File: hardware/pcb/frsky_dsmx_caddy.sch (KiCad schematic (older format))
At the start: 26 parts, among them P1 G9X, P2 Fr-Sky, P3 DSMX, Q1 BC847C, Q2 Si2319DS, Q3 Si2319DS, Q4 BC847C, U1 78L05, U2 LN-6206-30

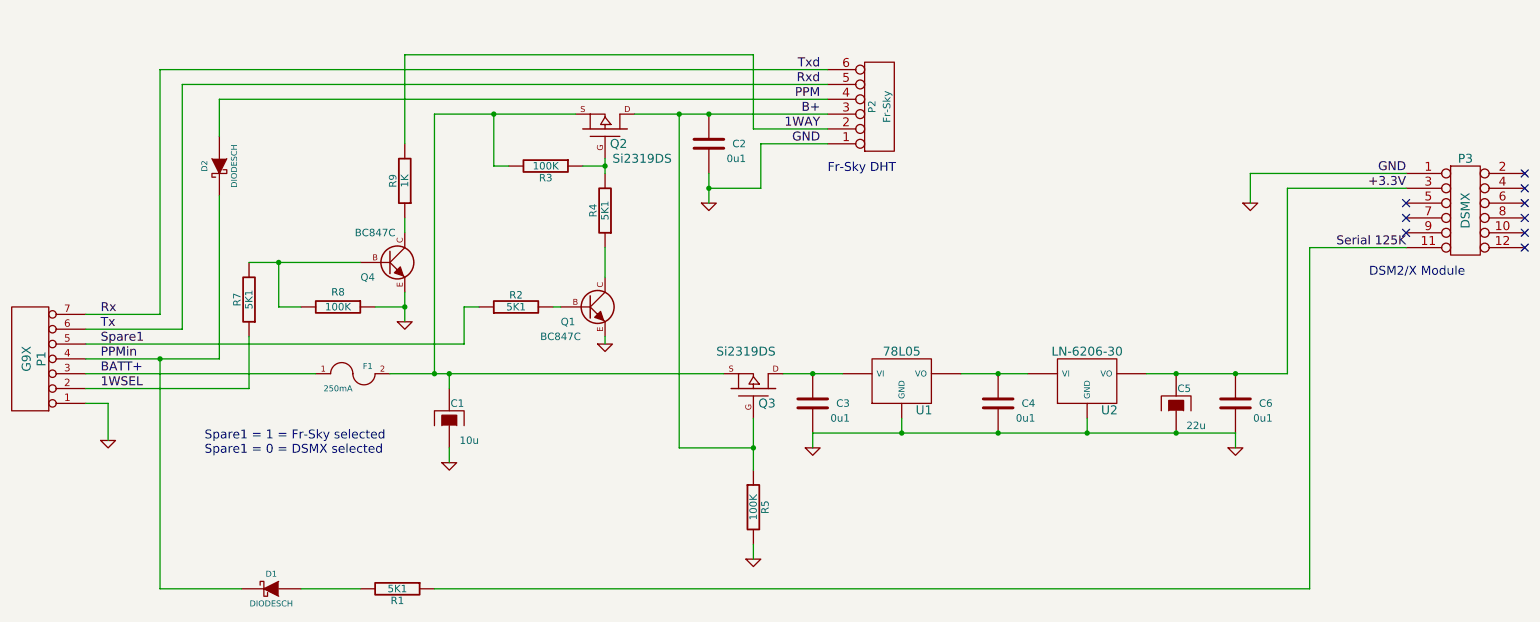
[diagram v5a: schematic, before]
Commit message: TX_CADDY changes to v1.4.
Essentially, this project is a right, royal FAILURE at this time. However,
the circuitry as presented in this commit _appears_ to function correctly
electrically, I have been unable to get the only available DSMX module
to operate. I am unwillingly to break my working DSM2 module in order
to test that it works -- though I presume it would, if the CRO readings
are to be believed.
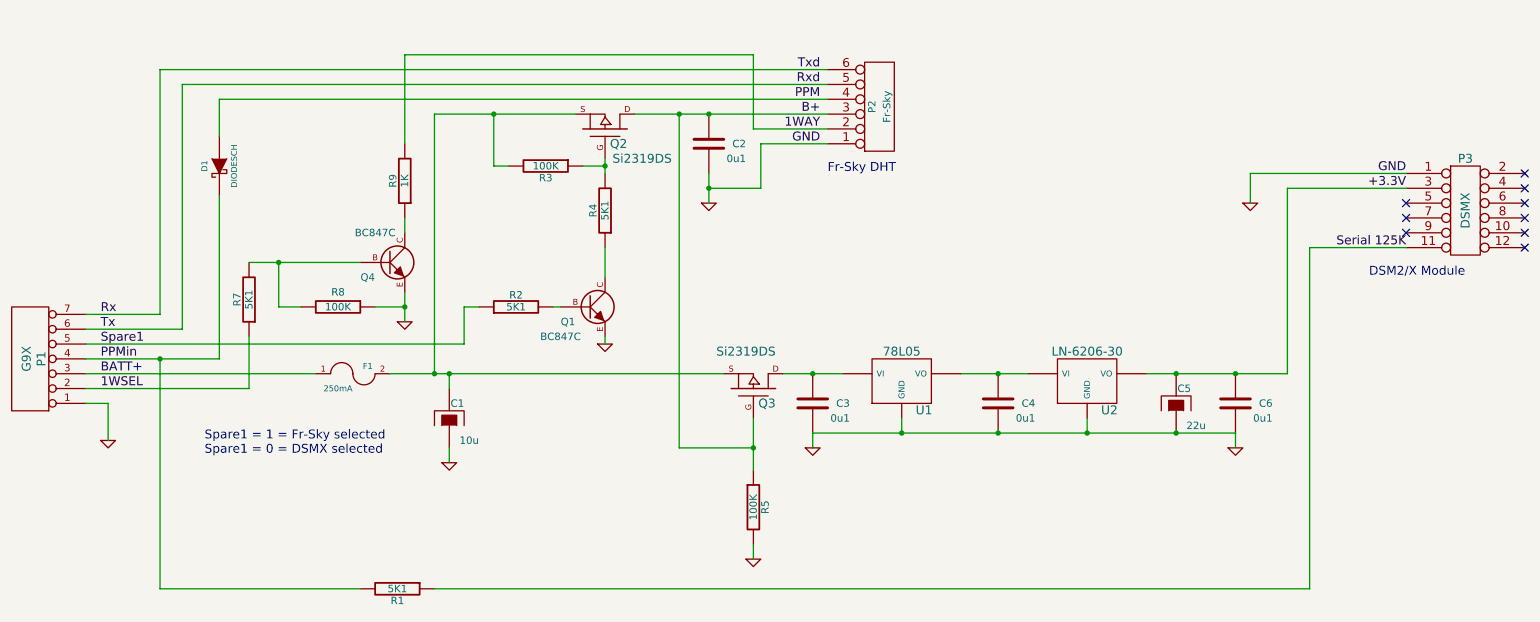
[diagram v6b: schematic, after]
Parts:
- removed D1: DIODESCH, symbol DIODESCH
- renumbered D2 to D1
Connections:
- net PPMin: now also R1.2
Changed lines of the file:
@@
-EESchema Schematic File Version 2  date Wed 24 Oct 2012 07:34:05 PM NZDT
+EESchema Schematic File Version 2  date Wed 24 Oct 2012 09:41:36 PM NZDT
 LIBS:gruvin
 LIBS:power
@@
 Title "Fr-Sky / DSMX TX Moudle Caddy"
 Date "24 oct 2012"
-Rev "1.3"
+Rev "1.4"
 Comp ""
 Comment1 ""
@@
 $EndDescr
 Wire Wire Line
+	1750 3400 1750 4950
+Wire Wire Line
+	1750 4950 3100 4950
+Connection ~ 5750 4000
+Wire Wire Line
+	5750 4000 5250 4000
+Wire Wire Line
+	5750 4150 5750 3800
+Wire Wire Line
+	4450 3050 4400 3050
+Wire Wire Line
+	5550 3500 3300 3500
+Connection ~ 3400 3050
+Wire Wire Line
+	3200 3050 3400 3050
+Wire Wire Line
+	6250 1850 5750 1850
+Wire Wire Line
+	5750 1850 5750 1350
+Wire Wire Line
+	5750 1350 3400 1350
+Wire Wire Line
+	3400 1350 3400 1950
+Wire Wire Line
+	3400 2550 3400 2450
+Wire Wire Line
+	3400 3150 3400 2950
+Wire Wire Line
+	6250 1950 5800 1950
+Connection ~ 4000 1750
+Wire Wire Line
+	4000 1750 4000 2100
+Wire Wire Line
+	4000 2100 4100 2100
+Wire Wire Line
+	5800 1950 5800 2250
+Wire Wire Line
+	6750 3800 6750 3900
+Connection ~ 5450 1750
+Wire Wire Line
+	5800 2250 5450 2250
+Wire Wire Line
+	1400 3950 1400 3700
+Wire Wire Line
+	1400 3700 1250 3700
+Wire Wire Line
+	5950 3500 6350 3500
+Wire Wire Line
+	2150 1900 2150 1650
+Connection ~ 8000 3900
+Wire Wire Line
+	10150 2250 9350 2250
+Wire Wire Line
+	9350 2250 9350 3500
+Wire Wire Line
+	1250 3200 1900 3200
+Wire Wire Line
+	1900 3200 1900 1550
+Wire Wire Line
+	1900 1550 6250 1550
+Wire Wire Line
+	1250 3400 2150 3400
+Wire Wire Line
+	2150 1650 6250 1650
+Connection ~ 4750 2100
+Wire Wire Line
+	4600 2100 4750 2100
+Connection ~ 3600 3500
+Wire Wire Line
+	3600 3500 3600 1750
+Connection ~ 7400 3500
+Wire Wire Line
+	8000 3900 8000 3800
+Wire Wire Line
+	4950 1750 6250 1750
+Connection ~ 7400 3900
+Connection ~ 6150 3500
+Connection ~ 6750 3900
+Wire Wire Line
+	4750 2150 4750 2050
+Wire Wire Line
+	3600 1750 4550 1750
+Wire Wire Line
+	9350 3500 8400 3500
+Wire Wire Line
+	3700 3600 3700 3500
+Wire Wire Line
+	7150 3500 7600 3500
+Connection ~ 3700 3500
+Wire Wire Line
+	1250 3500 2800 3500
+Wire Wire Line
+	1250 3100 1750 3100
+Wire Wire Line
+	1750 3100 1750 1450
+Wire Wire Line
+	1750 1450 6250 1450
+Wire Wire Line
+	9100 2350 9100 2150
+Wire Wire Line
+	9100 2150 10150 2150
+Wire Wire Line
+	2150 3400 2150 2300
+Connection ~ 1750 3400
+Wire Wire Line
+	9000 3900 6150 3900
+Connection ~ 9000 3500
+Connection ~ 8600 3500
+Connection ~ 8600 3900
+Wire Wire Line
+	3700 4000 3700 4100
+Wire Wire Line
+	9000 3900 9000 4000
+Wire Wire Line
+	6150 3900 6150 4000
+Connection ~ 5450 2250
+Wire Wire Line
+	5450 2350 5450 2150
+Wire Wire Line
+	1250 3300 3800 3300
+Wire Wire Line
+	3900 3050 3800 3050
+Wire Wire Line
+	10150 2650 9500 2650
+Wire Wire Line
+	9500 2650 9500 4950
+Wire Wire Line
+	9500 4950 3600 4950
+Wire Wire Line
+	1250 3600 2350 3600
+Wire Wire Line
+	2350 3600 2350 3250
+Wire Wire Line
+	2350 2750 3100 2750
+Wire Wire Line
+	2700 3050 2550 3050
+Wire Wire Line
+	2550 3050 2550 2750
+Connection ~ 2550 2750
+Wire Wire Line
+	3800 3050 3800 3300
+Wire Wire Line
+	4750 3250 4750 3300
+Wire Wire Line
+	4750 2650 4750 2850
+Wire Wire Line
+	5250 4000 5250 1750
+Connection ~ 5250 1750
+Wire Wire Line
 	5750 4750 5750 4650
-Connection ~ 5250 1750
-Wire Wire Line
-	5250 1750 5250 4000
-Wire Wire Line
-	4750 2650 4750 2850
-Wire Wire Line
-	4750 3250 4750 3300
-Wire Wire Line
-	3800 3050 3800 3300
-Connection ~ 2550 2750
-Wire Wire Line
-	2550 2750 2550 3050
-Wire Wire Line
-	2550 3050 2700 3050
-Wire Wire Line
-	2350 2750 2550 2750
-Wire Wire Line
-	2550 2750 3100 2750
-Wire Wire Line
-	2350 3250 2350 3600
-Wire Wire Line
-	2350 3600 1250 3600
-Wire Wire Line
-	3600 4950 9500 4950
-Wire Wire Line
-	9500 4950 9500 2650
-Wire Wire Line
-	9500 2650 10150 2650
-Wire Wire Line
-	3800 3050 3900 3050
-Wire Wire Line
-	3800 3300 1250 3300
-Wire Wire Line
-	5450 2350 5450 2250
-Wire Wire Line
-	5450 2250 5450 2150
-Connection ~ 5450 2250
-Wire Wire Line
-	6150 4000 6150 3900
-Wire Wire Line
-	9000 4000 9000 3900
-Wire Wire Line
-	3700 4000 3700 4100
-Wire Wire Line
-	1750 3400 1750 4950
-Wire Wire Line
-	1750 4950 2300 4950
-Connection ~ 8600 3900
-Connection ~ 8600 3500
-Connection ~ 9000 3500
-Wire Wire Line
-	9000 3900 8600 3900
-Wire Wire Line
-	8600 3900 8000 3900
-Wire Wire Line
-	8000 3900 7400 3900
-Wire Wire Line
-	7400 3900 6750 3900
-Wire Wire Line
-	6750 3900 6150 3900
-Connection ~ 1750 3400
-Wire Wire Line
-	2150 2300 2150 3400
-Wire Wire Line
-	10150 2150 9100 2150
-Wire Wire Line
-	9100 2150 9100 2350
-Wire Wire Line
-	6250 1450 1750 1450
-Wire Wire Line
-	1750 1450 1750 3100
-Wire Wire Line
-	1750 3100 1250 3100
-Wire Wire Line
-	1250 3500 2800 3500
-Connection ~ 3700 3500
-Wire Wire Line
-	7150 3500 7400 3500
-Wire Wire Line
-	7400 3500 7600 3500
-Wire Wire Line
-	3700 3500 3700 3600
-Wire Wire Line
-	8400 3500 8600 3500
-Wire Wire Line
-	8600 3500 9000 3500
-Wire Wire Line
-	9000 3500 9350 3500
-Wire Wire Line
-	4550 1750 4000 1750
-Wire Wire Line
-	4000 1750 3600 1750
-Wire Wire Line
-	4750 2150 4750 2100
-Wire Wire Line
-	4750 2100 4750 2050
-Connection ~ 6750 3900
-Connection ~ 6150 3500
-Connection ~ 7400 3900
-Wire Wire Line
-	4950 1750 5250 1750
-Wire Wire Line
-	5250 1750 5450 1750
-Wire Wire Line
-	5450 1750 6250 1750
-Wire Wire Line
-	8000 3900 8000 3800
-Connection ~ 7400 3500
-Wire Wire Line
-	3600 1750 3600 3500
-Connection ~ 3600 3500
-Wire Wire Line
-	4600 2100 4750 2100
-Connection ~ 4750 2100
-Wire Wire Line
-	6250 1650 2150 1650
-Wire Wire Line
-	2150 3400 1750 3400
-Wire Wire Line
-	1750 3400 1250 3400
-Wire Wire Line
-	6250 1550 1900 1550
-Wire Wire Line
-	1900 1550 1900 3200
-Wire Wire Line
-	1900 3200 1250 3200
-Wire Wire Line
-	9350 3500 9350 2250
-Wire Wire Line
-	9350 2250 10150 2250
-Connection ~ 8000 3900
-Wire Wire Line
-	2150 1650 2150 1900
-Wire Wire Line
-	5950 3500 6150 3500
-Wire Wire Line
-	6150 3500 6350 3500
-Wire Wire Line
-	3100 4950 2700 4950
-Wire Wire Line
-	1250 3700 1400 3700
-Wire Wire Line
-	1400 3700 1400 3950
-Wire Wire Line
-	5450 2250 5800 2250
-Connection ~ 5450 1750
-Wire Wire Line
-	6750 3800 6750 3900
-Wire Wire Line
-	5800 2250 5800 1950
-Wire Wire Line
-	4100 2100 4000 2100
-Wire Wire Line
-	4000 2100 4000 1750
-Connection ~ 4000 1750
-Wire Wire Line
-	5800 1950 6250 1950
-Wire Wire Line
-	3400 3150 3400 3050
-Wire Wire Line
-	3400 3050 3400 2950
-Wire Wire Line
-	3400 2550 3400 2450
-Wire Wire Line
-	3400 1950 3400 1350
-Wire Wire Line
-	3400 1350 5750 1350
-Wire Wire Line
-	5750 1350 5750 1850
-Wire Wire Line
-	5750 1850 6250 1850
-Wire Wire Line
-	3200 3050 3400 3050
-Connection ~ 3400 3050
-Wire Wire Line
-	5550 3500 3700 3500
-Wire Wire Line
-	3700 3500 3600 3500
-Wire Wire Line
-	3600 3500 3300 3500
-Wire Wire Line
-	4450 3050 4400 3050
-Wire Wire Line
-	5750 4150 5750 4000
-Wire Wire Line
-	5750 4000 5750 3800
-Wire Wire Line
-	5250 4000 5750 4000
-Connection ~ 5750 4000
-$Comp
-L GND #PWR?
+$Comp
+L GND #PWR01
 U 1 1 50878285
 P 5750 4750
-F 0 "#PWR?" H 5750 4750 30  0001 C CNN
+F 0 "#PWR01" H 5750 4750 30  0001 C CNN
 F 1 "GND" H 5750 4680 30  0001 C CNN
 	1    5750 4750
@@
 $EndComp
 $Comp
-L GND #PWR2
+L GND #PWR02
 U 1 1 50627C0D
 P 3400 3150
-F 0 "#PWR2" H 3400 3150 30  0001 C CNN
+F 0 "#PWR02" H 3400 3150 30  0001 C CNN
 F 1 "GND" H 3400 3080 30  0001 C CNN
 	1    3400 3150
@@
 NoConn ~ 10150 2550
 $Comp
-L GND #PWR8
+L GND #PWR03
 U 1 1 504D1983
 P 9000 4000
-F 0 "#PWR8" H 9000 4000 30  0001 C CNN
+F 0 "#PWR03" H 9000 4000 30  0001 C CNN
 F 1 "GND" H 9000 3930 30  0001 C CNN
 	1    9000 4000
@@
 $EndComp
 $Comp
-L GND #PWR3
+L GND #PWR04
 U 1 1 504D1897
 P 3700 4100
-F 0 "#PWR3" H 3700 4100 30  0001 C CNN
+F 0 "#PWR04" H 3700 4100 30  0001 C CNN
 F 1 "GND" H 3700 4030 30  0001 C CNN
 	1    3700 4100
@@
 $Comp
 L DIODESCH D1
-U 1 1 504D150C
-P 2500 4950
-F 0 "D1" H 2500 5050 40  0000 C CNN
-F 1 "DIODESCH" H 2500 4850 40  0000 C CNN
-	1    2500 4950
-	-1   0    0    -1
-$EndComp
-$Comp
-L DIODESCH D2
 U 1 1 504D14E4
 P 2150 2100
-F 0 "D2" H 2150 2200 40  0000 C CNN
+F 0 "D1" H 2150 2200 40  0000 C CNN
 F 1 "DIODESCH" H 2150 2000 40  0000 C CNN
 	1    2150 2100
@@
 $EndComp
 $Comp
-L GND #PWR9
+L GND #PWR05
 U 1 1 504D13B3
 P 9100 2350
-F 0 "#PWR9" H 9100 2350 30  0001 C CNN
+F 0 "#PWR05" H 9100 2350 30  0001 C CNN
 F 1 "GND" H 9100 2280 30  0001 C CNN
 	1    9100 2350
@@
 PPMin
 $Comp
-L GND #PWR5
+L GND #PWR06
 U 1 1 504D1165
 P 5450 2350
-F 0 "#PWR5" H 5450 2350 30  0001 C CNN
+F 0 "#PWR06" H 5450 2350 30  0001 C CNN
 F 1 "GND" H 5450 2280 30  0001 C CNN
 	1    5450 2350
@@
 BATT+
 $Comp
-L GND #PWR1
+L GND #PWR07
 U 1 1 504D1086
 P 1400 3950
-F 0 "#PWR1" H 1400 3950 30  0001 C CNN
+F 0 "#PWR07" H 1400 3950 30  0001 C CNN
 F 1 "GND" H 1400 3880 30  0001 C CNN
 	1    1400 3950
@@
 $EndComp
 $Comp
-L GND #PWR4
+L GND #PWR08
 U 1 1 4E7B4B20
 P 4750 3300
-F 0 "#PWR4" H 4750 3300 30  0001 C CNN
+F 0 "#PWR08" H 4750 3300 30  0001 C CNN
 F 1 "GND" H 4750 3230 30  0001 C CNN
 	1    4750 3300
@@
 $EndComp
 $Comp
-L GND #PWR7
+L GND #PWR09
 U 1 1 4E1493B8
 P 6150 4000
-F 0 "#PWR7" H 6150 4000 30  0001 C CNN
+F 0 "#PWR09" H 6150 4000 30  0001 C CNN
 F 1 "GND" H 6150 3930 30  0001 C CNN
 	1    6150 4000

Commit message: TX_CADDY (the saga continues)
The comedy of oversights, stuff-ups and general failures to get a rediculously
simple circuit to work properly continues. This time we introduce a 5V reg
that can actually handle the task reliably. :-/
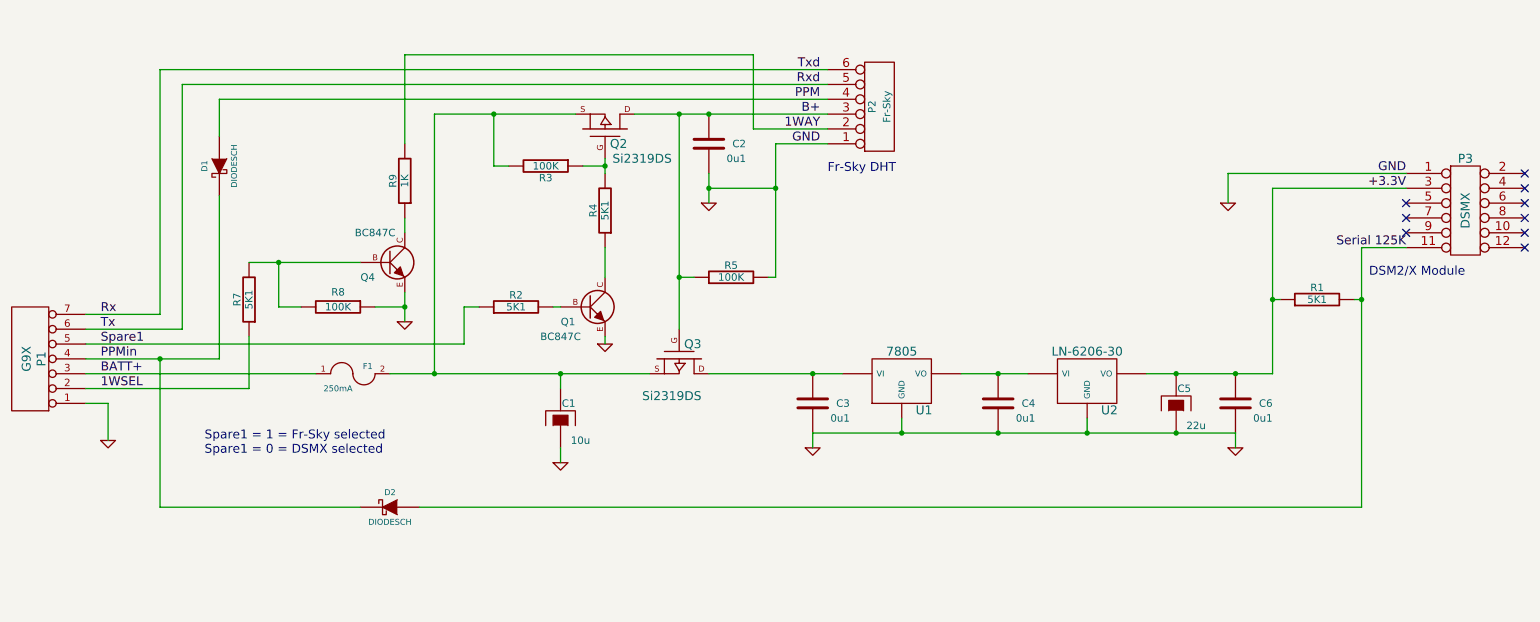
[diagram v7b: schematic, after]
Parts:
- added D2: DIODESCH, symbol DIODESCH
- U1: value 78L05 -> 7805; footprint SOT89 -> TO220
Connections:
- net +3.3V: now also R1.1
- net PPMin: now also D2.2 (K); no longer R1.2
- net Serial 125K: now also R1.2, D2.1 (A); no longer R1.1
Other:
- moved on the sheet: C1, Q3, R5
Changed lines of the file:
@@
-EESchema Schematic File Version 2  date Wed 24 Oct 2012 09:41:36 PM NZDT
+EESchema Schematic File Version 2  date Sat 27 Oct 2012 12:35:31 AM NZDT
 LIBS:gruvin
 LIBS:power
@@
 Sheet 1 1
 Title "Fr-Sky / DSMX TX Moudle Caddy"
-Date "24 oct 2012"
-Rev "1.4"
+Date "26 oct 2012"
+Rev "2.0"
 Comp ""
 Comment1 ""
@@
 Comment4 "Licensed under the TAPR Open Hardware License (see file,  LICENSE)"
 $EndDescr
-Wire Wire Line
-	1750 3400 1750 4950
-Wire Wire Line
-	1750 4950 3100 4950
-Connection ~ 5750 4000
-Wire Wire Line
-	5750 4000 5250 4000
-Wire Wire Line
-	5750 4150 5750 3800
+Connection ~ 9850 3000
+Wire Wire Line
+	9800 3000 9850 3000
+Connection ~ 5900 2250
+Wire Wire Line
+	5900 2850 5900 1950
+Wire Wire Line
+	5900 2850 5850 2850
+Wire Wire Line
+	1750 3400 1750 4400
+Wire Wire Line
+	1750 4400 3100 4400
 Wire Wire Line
 	4450 3050 4400 3050
 Wire Wire Line
-	5550 3500 3300 3500
+	5050 3500 3300 3500
 Connection ~ 3400 3050
 Wire Wire Line
@@
 	3400 3150 3400 2950
 Wire Wire Line
-	6250 1950 5800 1950
+	5900 1950 6250 1950
 Connection ~ 4000 1750
 Wire Wire Line
@@
 Wire Wire Line
 	4000 2100 4100 2100
-Wire Wire Line
-	5800 1950 5800 2250
 Wire Wire Line
 	6750 3800 6750 3900
 Connection ~ 5450 1750
 Wire Wire Line
-	5800 2250 5450 2250
+	5450 2250 5900 2250
 Wire Wire Line
 	1400 3950 1400 3700
@@
 	1400 3700 1250 3700
 Wire Wire Line
-	5950 3500 6350 3500
+	5450 3500 6350 3500
 Wire Wire Line
 	2150 1900 2150 1650
 Connection ~ 8000 3900
 Wire Wire Line
-	10150 2250 9350 2250
-Wire Wire Line
-	9350 2250 9350 3500
+	10150 2250 9250 2250
+Wire Wire Line
+	9250 2250 9250 3500
 Wire Wire Line
 	1250 3200 1900 3200
@@
 	3600 1750 4550 1750
 Wire Wire Line
-	9350 3500 8400 3500
-Wire Wire Line
-	3700 3600 3700 3500
+	9250 3500 8400 3500
+Wire Wire Line
+	4450 3600 4450 3500
 Wire Wire Line
 	7150 3500 7600 3500
-Connection ~ 3700 3500
+Connection ~ 4450 3500
 Wire Wire Line
 	1250 3500 2800 3500
@@
 	1750 1450 6250 1450
 Wire Wire Line
-	9100 2350 9100 2150
-Wire Wire Line
-	9100 2150 10150 2150
+	8950 2350 8950 2150
+Wire Wire Line
+	8950 2150 10150 2150
 Wire Wire Line
 	2150 3400 2150 2300
@@
 Connection ~ 8600 3900
 Wire Wire Line
-	3700 4000 3700 4100
+	4450 4000 4450 4100
 Wire Wire Line
 	9000 3900 9000 4000
@@
 	3900 3050 3800 3050
 Wire Wire Line
-	10150 2650 9500 2650
-Wire Wire Line
-	9500 2650 9500 4950
-Wire Wire Line
-	9500 4950 3600 4950
+	10150 2650 9850 2650
+Wire Wire Line
+	9850 2650 9850 4400
+Wire Wire Line
+	9850 4400 3500 4400
 Wire Wire Line
 	1250 3600 2350 3600
@@
 Wire Wire Line
 	4750 2650 4750 2850
-Wire Wire Line
-	5250 4000 5250 1750
 Connection ~ 5250 1750
 Wire Wire Line
-	5750 4750 5750 4650
-$Comp
-L GND #PWR01
-U 1 1 50878285
-P 5750 4750
-F 0 "#PWR01" H 5750 4750 30  0001 C CNN
-F 1 "GND" H 5750 4680 30  0001 C CNN
-	1    5750 4750
-	1    0    0    -1
+	5350 2850 5250 2850
+Connection ~ 5250 2850
+Wire Wire Line
+	5250 3200 5250 1750
+Wire Wire Line
+	9300 3000 9250 3000
+Connection ~ 9250 3000
+$Comp
+L R R1
+U 1 1 508A6768
+P 9550 3000
+F 0 "R1" V 9630 3000 50  0000 C CNN
+F 1 "5K1" V 9550 3000 50  0000 C CNN
+	1    9550 3000
+	0    -1   -1   0
+$EndComp
+$Comp
+L DIODESCH D2
+U 1 1 508A66B2
+P 3300 4400
+F 0 "D2" H 3300 4500 40  0000 C CNN
+F 1 "DIODESCH" H 3300 4300 40  0000 C CNN
+	1    3300 4400
+	-1   0    0    -1
 $EndComp
 $Comp
 L R R5
 U 1 1 50877F34
-P 5750 4400
-F 0 "R5" V 5830 4400 50  0000 C CNN
-F 1 "100K" V 5750 4400 50  0000 C CNN
-	1    5750 4400
-	1    0    0    -1
+P 5600 2850
+F 0 "R5" V 5680 2850 50  0000 C CNN
+F 1 "100K" V 5600 2850 50  0000 C CNN
+	1    5600 2850
+	0    -1   -1   0
 $EndComp
 Text Label 1350 3600 0    60   ~ 0
@@
 $EndComp
 $Comp
-L GND #PWR02
+L GND #PWR01
 U 1 1 50627C0D
 P 3400 3150
-F 0 "#PWR02" H 3400 3150 30  0001 C CNN
+F 0 "#PWR01" H 3400 3150 30  0001 C CNN
 F 1 "GND" H 3400 3080 30  0001 C CNN
 	1    3400 3150
@@
 NoConn ~ 10150 2550
 $Comp
-L GND #PWR03
+L GND #PWR02
 U 1 1 504D1983
 P 9000 4000
-F 0 "#PWR03" H 9000 4000 30  0001 C CNN
+F 0 "#PWR02" H 9000 4000 30  0001 C CNN
 F 1 "GND" H 9000 3930 30  0001 C CNN
 	1    9000 4000
@@
 $EndComp
 $Comp
-L GND #PWR04
+L GND #PWR03
 U 1 1 504D1897
-P 3700 4100
-F 0 "#PWR04" H 3700 4100 30  0001 C CNN
-F 1 "GND" H 3700 4030 30  0001 C CNN
-	1    3700 4100
+P 4450 4100
+F 0 "#PWR03" H 4450 4100 30  0001 C CNN
+F 1 "GND" H 4450 4030 30  0001 C CNN
+	1    4450 4100
 	1    0    0    -1
 $EndComp
@@
 $EndComp
 $Comp
-L R R1
-U 1 1 504D1401
-P 3350 4950
-F 0 "R1" V 3430 4950 50  0000 C CNN
-F 1 "5K1" V 3350 4950 50  0000 C CNN
-	1    3350 4950
-	0    1    1    0
-$EndComp
-$Comp
-L GND #PWR05
+L GND #PWR04
 U 1 1 504D13B3
-P 9100 2350
-F 0 "#PWR05" H 9100 2350 30  0001 C CNN
-F 1 "GND" H 9100 2280 30  0001 C CNN
-	1    9100 2350
+P 8950 2350
+F 0 "#PWR04" H 8950 2350 30  0001 C CNN
+F 1 "GND" H 8950 2280 30  0001 C CNN
+	1    8950 2350
 	1    0    0    -1
 $EndComp
@@
 PPMin
 $Comp
-L GND #PWR06
+L GND #PWR05
 U 1 1 504D1165
 P 5450 2350
-F 0 "#PWR06" H 5450 2350 30  0001 C CNN
+F 0 "#PWR05" H 5450 2350 30  0001 C CNN
 F 1 "GND" H 5450 2280 30  0001 C CNN
 	1    5450 2350
@@
 BATT+
 $Comp
-L GND #PWR07
+L GND #PWR06
 U 1 1 504D1086
 P 1400 3950
-F 0 "#PWR07" H 1400 3950 30  0001 C CNN
+F 0 "#PWR06" H 1400 3950 30  0001 C CNN
 F 1 "GND" H 1400 3880 30  0001 C CNN
 	1    1400 3950
@@
 L MOSFET_P Q3
 U 1 1 504D0D5B
-P 5750 3600
-F 0 "Q3" V 5650 3750 60  0000 R CNN
-F 1 "Si2319DS" V 6000 3750 60  0000 R CNN
-	1    5750 3600
-	0    1    -1   0
+P 5250 3400
+F 0 "Q3" V 5150 3550 60  0000 R CNN
+F 1 "Si2319DS" V 5500 3550 60  0000 R CNN
+	1    5250 3400
+	0    1    1    0
 $EndComp
 $Comp
 L CAPAPOL C1
 U 1 1 504D0AFE
-P 3700 3800
-F 0 "C1" H 3600 3700 50  0000 L CNN
-F 1 "10u" H 3500 3950 50  0000 L CNN
-	1    3700 3800
+P 4450 3800
+F 0 "C1" H 4350 3700 50  0000 L CNN
+F 1 "10u" H 4250 3950 50  0000 L CNN
+	1    4450 3800
 	-1   0    0    1
 $EndComp
@@
 $EndComp
 $Comp
-L GND #PWR08
+L GND #PWR07
 U 1 1 4E7B4B20
 P 4750 3300
-F 0 "#PWR08" H 4750 3300 30  0001 C CNN
+F 0 "#PWR07" H 4750 3300 30  0001 C CNN
 F 1 "GND" H 4750 3230 30  0001 C CNN
 	1    4750 3300
@@
 P 6750 3550
 F 0 "U1" H 6900 3354 60  0000 C CNN
-F 1 "78L05" H 6750 3750 60  0000 C CNN
-F 2 "SOT89" H 6960 3294 60  0001 C CNN
+F 1 "7805" H 6750 3750 60  0000 C CNN
+F 2 "TO220" H 6960 3294 60  0001 C CNN
 	1    6750 3550
 	1    0    0    -1
@@
 $EndComp
 $Comp
-L GND #PWR09
+L GND #PWR08
 U 1 1 4E1493B8
 P 6150 4000
-F 0 "#PWR09" H 6150 4000 30  0001 C CNN
+F 0 "#PWR08" H 6150 4000 30  0001 C CNN
 F 1 "GND" H 6150 3930 30  0001 C CNN
 	1    6150 4000
